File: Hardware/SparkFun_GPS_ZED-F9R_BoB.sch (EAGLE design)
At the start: 82 parts, among them J1 U.FL, J3 QWIIC_RIGHT_ANGLE, J4 QWIIC_RIGHT_ANGLE, U1 UBLOX_ZED_F9R, U2 3.3V, U4 HCPL-270L

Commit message: Renumbers parts, updates parts with PROD_IDs that didn't have them before
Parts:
- removed C12, C15: 1nF, SparkFun-Capacitors:1.0NF/1000PF-0402-25V-10%-X7R
- removed C16: 0.1uF, SparkFun-Capacitors:0.1UF-0402-6.3V-10%-X7R
- removed D10, D9: 0.5A/40V/420mV, classified:BZX84_DIODE
- removed R35, R37: 3.3k, SparkFun-Resistors:3.3KOHM-0603-1/10W-1%
- removed R36, R38: 470, SparkFun-Resistors:470OHM-0603-1/10W-1%
- removed R39, R40: 910, classified:910OHM-0603-1/10W-5%
- removed U$63: UHS_INVERTER_SCHMITT_TRIGGERSIP6, classified:UHS_INVERTER_SCHMITT_TRIGGERSIP6
- added C10, C9: 1.0uF, SparkFun-Capacitors:1.0UF-0603-16V-10%-X7R
- added C8: 47pF, SparkFun-Capacitors:47PF-0402-25V-5%-X7R
- added D7: BLUE, SparkFun-LED:LED-BLUE0603
- added D8: 0.5A/40V/420mV, SparkFun-DiscreteSemi:DIODE-SCHOTTKY-PMEG4005EJ
- added R29, R30: 1KOHM-0402-1/16W-1%, SparkFun-Resistors:1KOHM-0402-1/16W-1%
- added R31, R32: 27, SparkFun-Resistors:27OHM-0603-1/10W-1%
- added R33: 2.2K, SparkFun-Resistors:2.2KOHM-0402-1/16W-1%
- added R34: 3.3k, SparkFun-Resistors:3.3KOHM-0603-1/10W-1%
- added U5: 3.3V, SparkFun-IC-Power:V_REG_AP2112K-3.3V
- C1: value 1.0uF -> 0.1uF; device SparkFun-Capacitors:1.0UF-0603-16V-10%-X7R -> SparkFun-Capacitors:0.1UF-0402-6.3V-10%-X7R
- C2: value 47pF -> 1.0uF; device SparkFun-Capacitors:47PF-0402-25V-5%-X7R -> SparkFun-Capacitors:1.0UF-0603-16V-10%-X7R
- C3, C4: value 1.0uF -> 1nF; device SparkFun-Capacitors:1.0UF-0603-16V-10%-X7R -> SparkFun-Capacitors:1.0NF/1000PF-0402-25V-10%-X7R
- D1: value RED -> 0.5A/40V/420mV; device SparkFun-LED:LED-RED0603 -> classified:BZX84_DIODE
- D2: value BLUE -> 0.5A/40V/420mV; device SparkFun-LED:LED-BLUE0603 -> classified:BZX84_DIODE
- D3: value BLUE -> PRTR5V0U2F; device SparkFun-LED:LED-BLUE0603 -> SparkFun-IC-Power:PRTR5V0U2F
- D4: value BLUE -> RED; device SparkFun-LED:LED-BLUE0603 -> SparkFun-LED:LED-RED0603
- D5: value PRTR5V0U2F -> BLUE; device SparkFun-IC-Power:PRTR5V0U2F -> SparkFun-LED:LED-BLUE0603
- D6: value 0.5A/40V/420mV -> BLUE; device SparkFun-DiscreteSemi:DIODE-SCHOTTKY-PMEG4005EJ -> SparkFun-LED:LED-BLUE0603
- R1: value 100K -> 3.3k; device SparkFun-Resistors:100KOHM-0402-1/16W-1% -> SparkFun-Resistors:3.3KOHM-0603-1/10W-1%
- R17: device SparkFun-Resistors:33OHM-0603-1/10W-1% -> SparkFun-Resistors:33OHM-0402-1/10W-1%
- R18, R20: value 5.1k -> 33; device SparkFun-Resistors:5.1KOHM-0402-1/16W-1% -> SparkFun-Resistors:33OHM-0402-1/10W-1%
- R19: value 2.2K -> 33; device SparkFun-Resistors:2.2KOHM-0402-1/16W-1% -> SparkFun-Resistors:33OHM-0402-1/10W-1%
- R2: value 33 -> 3.3k; device SparkFun-Resistors:33OHM-0402-1/10W-1% -> SparkFun-Resistors:3.3KOHM-0603-1/10W-1%
- R21, R22: value 1KOHM-0402-1/16W-1% -> 33; device SparkFun-Resistors:1KOHM-0402-1/16W-1% -> SparkFun-Resistors:33OHM-0402-1/10W-1%
- R23: value 1KOHM-0402-1/16W-1% -> 33; device SparkFun-Resistors:1KOHM-0402-1/16W-1% -> SparkFun-Resistors:33OHM-0603-1/10W-1%
- R24: value 1KOHM-0402-1/16W-1% -> 5.1k; device SparkFun-Resistors:1KOHM-0402-1/16W-1% -> SparkFun-Resistors:5.1KOHM-0402-1/16W-1%
- R25: value 2.2K -> 5.1k; device SparkFun-Resistors:2.2KOHM-0402-1/16W-1% -> SparkFun-Resistors:5.1KOHM-0402-1/16W-1%
- R26: value 27 -> 2.2K; device SparkFun-Resistors:27OHM-0603-1/10W-1% -> SparkFun-Resistors:2.2KOHM-0402-1/16W-1%
- R27: value 27 -> 1KOHM-0402-1/16W-1%; device SparkFun-Resistors:27OHM-0603-1/10W-1% -> SparkFun-Resistors:1KOHM-0402-1/16W-1%
- R28: value 3.3k -> 1KOHM-0402-1/16W-1%; device SparkFun-Resistors:3.3KOHM-0603-1/10W-1% -> SparkFun-Resistors:1KOHM-0402-1/16W-1%
- R3: value 33 -> 100K; device SparkFun-Resistors:33OHM-0402-1/10W-1% -> SparkFun-Resistors:100KOHM-0402-1/16W-1%
- R4, R6: value 33 -> 910; device SparkFun-Resistors:33OHM-0402-1/10W-1% -> classified:910OHM-0603-1/10W-5%
- R5, R7: value 33 -> 470; device SparkFun-Resistors:33OHM-0402-1/10W-1% -> SparkFun-Resistors:470OHM-0603-1/10W-1%
- U1: value UBLOX_ZED_F9R -> HCPL-073L; device classified:UBLOX_ZED_F9R -> classified:HCPL-073L
- U2: value 3.3V -> UBLOX_ZED_F9R; device SparkFun-IC-Power:V_REG_AP2112K-3.3V -> classified:UBLOX_ZED_F9R
- U4: value HCPL-270L -> UHS_INVERTER_SCHMITT_TRIGGERSIP6; device classified:HCPL-270L -> classified:UHS_INVERTER_SCHMITT_TRIGGERSIP6
- renumbered $1_36_$_2020-02-13_17-32-45 to $1_25_$_2020-03-27_15-35-06, C17 to C6, C18 to C7, U$62 to U3
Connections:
- net !RESET: now also R10.2; no longer R4.2
- net !SAFEBOOT: now also R22.2; no longer R16.2
- net 3.3V: now also C10.1, C2.1, D4.A, D8.A, R3.2, R4.2, R6.2, U2.VCC, U2.V_USB, U5.OUT; no longer C16.1, C4.1, D1.A, D6.A, R1.2, R39.2, R40.2, U$63.VCC, U1.V_USB, U2.OUT
- net DIR+: now also R2.1; no longer R37.1
- net DIR_IN: now also R5.2, U1.ANODE2; no longer R38.2, U4.ANODE2
- net DIR_OUT: now also R9.1, U4.Y; no longer R3.1, U$63.Y
- net DIR_SCHMITT: now also R4.1, U1.VOUT2, U4.A; no longer R40.1, U$63.A, U4.VOUT2
- net DMINUS: now also R31.2, U2.USB_D-; no longer R26.2, U1.USB_D-
- net DPLUS: now also R32.2, U2.USB_D+; no longer R27.2, U1.USB_D+
- net D_SEL: now also U2.D_SEL; no longer U1.D_SEL
- net GEOF_STAT: now also D7.A, R19.2; no longer D4.A, R13.2
- net GND: now also C10.2, C8.2, C9.2, D1.A, D2.A, D3.2, R24.1, R25.1, R3.1, U1.CATHODE1, U1.CATHODE2, U5.GND; no longer C12.2, C15.2, C16.2, D10.A, D5.2, D9.A, R1.1, R18.1, R20.1, U$63.GND, U4.CATHODE1, U4.CATHODE2
- net INT: now also R11.2; no longer R5.2
- net N$1: now also R33.2; no longer R25.2
- net N$10: now also D3.4, R32.1; no longer D5.4, R27.1
- net N$11: now also R10.1, U2.!RESET!; no longer R4.1, U1.!RESET!
- net N$12: now also R11.1, U2.EXTINT; no longer R5.1, U1.EXTINT
- net N$14: now also R24.2; no longer R18.2
- net N$15: now also R25.2; no longer R20.2
- net N$16: now also R12.1, U2.SDA/!CS!; no longer R6.1, U1.SDA/!CS!
- net N$17: now also R13.1, U2.SCL/CLK; no longer R7.1, U1.SCL/CLK
- net N$18: now also R14.1, U2.TX_READY; no longer R8.1, U1.TX_READY
- net N$19: now also R15.1, U2.TX/MISO; no longer R9.1, U1.TX/MISO
- net N$2: now also D8.C, R34.2; no longer D6.C, R28.2
- net N$20: now also R16.1, U2.RX/MOSI; no longer R10.1, U1.RX/MOSI
- net N$21: now also R17.1, U2.TX2; no longer R11.1, U1.TX2
- net N$22: now also R29.1; no longer R23.1
- net N$23: now also R28.1; no longer R22.1
- net N$24: now also D5.C, R28.2; no longer D2.C, R22.2
- net N$25: now also D6.C, R29.2; no longer D3.C, R23.2
- net N$26: now also R18.1, U2.RX2; no longer R12.1, U1.RX2
- net N$27: now also R19.1, U2.GEO_FENCE_STAT; no longer R13.1, U1.GEO_FENCE_STAT
- net N$28: now also R20.1, U2.RTK_STAT; no longer R14.1, U1.RTK_STAT
- net N$29: now also R21.1, U2.TIMEPULSE; no longer R15.1, U1.TIMEPULSE
- net N$3: now also R26.2; no longer R19.2
- net N$30: now also R22.1, U2.!SAFEBOOT!; no longer R16.1, U1.!SAFEBOOT!
- net N$31: now also R8.2, U2.WHEEL_TKS; no longer R2.2, U1.WHEEL_TKS
- net N$32: now also R9.2, U2.DIR; no longer R3.2, U1.DIR
- net N$33: now also R30.1; no longer R24.1
- net N$34: now also D7.C, R30.2; no longer D4.C, R24.2
- net N$35: now also C4.1, D2.C, R1.2, R7.1; no longer C15.1, D9.C, R35.2, R36.1
- net N$37: now also C3.1, D1.C, R2.2, R5.1; no longer C12.1, D10.C, R37.2, R38.1
- net N$4: now also D4.C, R27.2; no longer D1.C, R21.2
- net N$5: now also C8.1, R23.1; no longer C2.1, R17.1
- net N$6: now also D3.3; no longer D5.3
- net N$7: now also D3.1; no longer D5.1
- net N$8: now also R27.1; no longer R21.1
- net N$9: now also D3.6, R31.1; no longer D5.6, R26.1
- net PPS: now also D5.A, R21.2; no longer D2.A, R15.2
- net RF_IN: now also U2.RF_IN; no longer U1.RF_IN
- net RTK_STAT: now also D6.A, R20.2; no longer D3.A, R14.2
- net RXI/MOSI: now also R16.2; no longer R10.2
- net RXI2: now also R18.2; no longer R12.2
- net SCL/CLK: now also R13.2, R26.1; no longer R19.1, R7.2
- net SDA/!CS: now also R12.2, R33.1; no longer R25.1, R6.2
- net TXO/MISO: now also R15.2; no longer R9.2
- net TXO2: now also R17.2; no longer R11.2
- net TX_READY: now also R14.2; no longer R8.2
- net VIN: now also C9.1, D3.5, U5.EN, U5.IN; no longer C3.1, D5.5, U2.EN, U2.IN
- net V_BATT: now also R34.1, U2.V_BKCP; no longer R28.1, U1.V_BKCP
- net V_RF: now also R23.2, U2.V_RF; no longer R17.2, U1.V_RF
- net WT+: now also R1.1; no longer R35.1
- net WT_IN: now also R7.2, U1.ANODE1; no longer R36.2, U4.ANODE1
- net WT_OUT: now also R8.1; no longer R2.1
- net WT_SCHMITT: now also R6.1, U1.VOUT1; no longer R39.1, U4.VOUT1
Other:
- moved on the sheet: C1, C2, C3, C4, D4, R1, R10, R11, R12, R13, R14, R15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

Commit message: Updates silk, fixes RF trace, moves some traces for better clearance
* Fixes various small design issues
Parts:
- renumbered JP1 to PWR, JP2 to PPS, JP3 to RTK, JP4 to GEOF
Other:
- note added: "Wheel Tick/Direction Input: 3-24V"

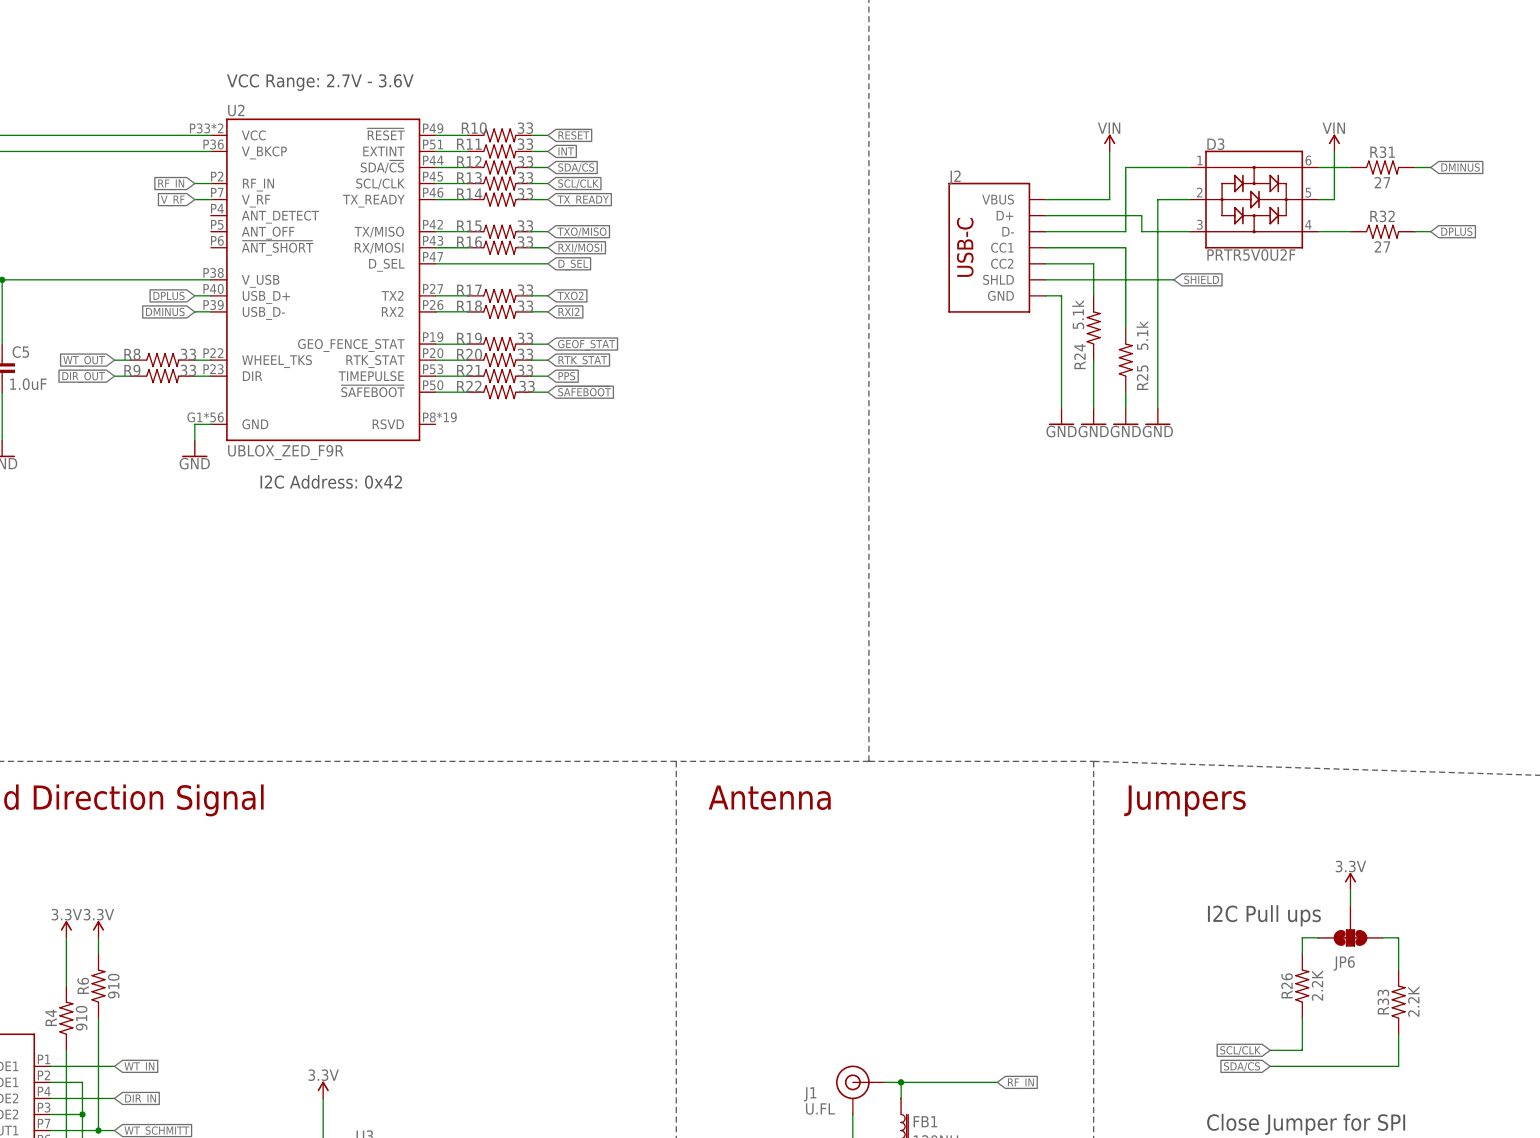
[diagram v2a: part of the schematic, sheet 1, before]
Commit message: Removes 0402 33 Ohm resistors in place of 33Ohm resistor bank
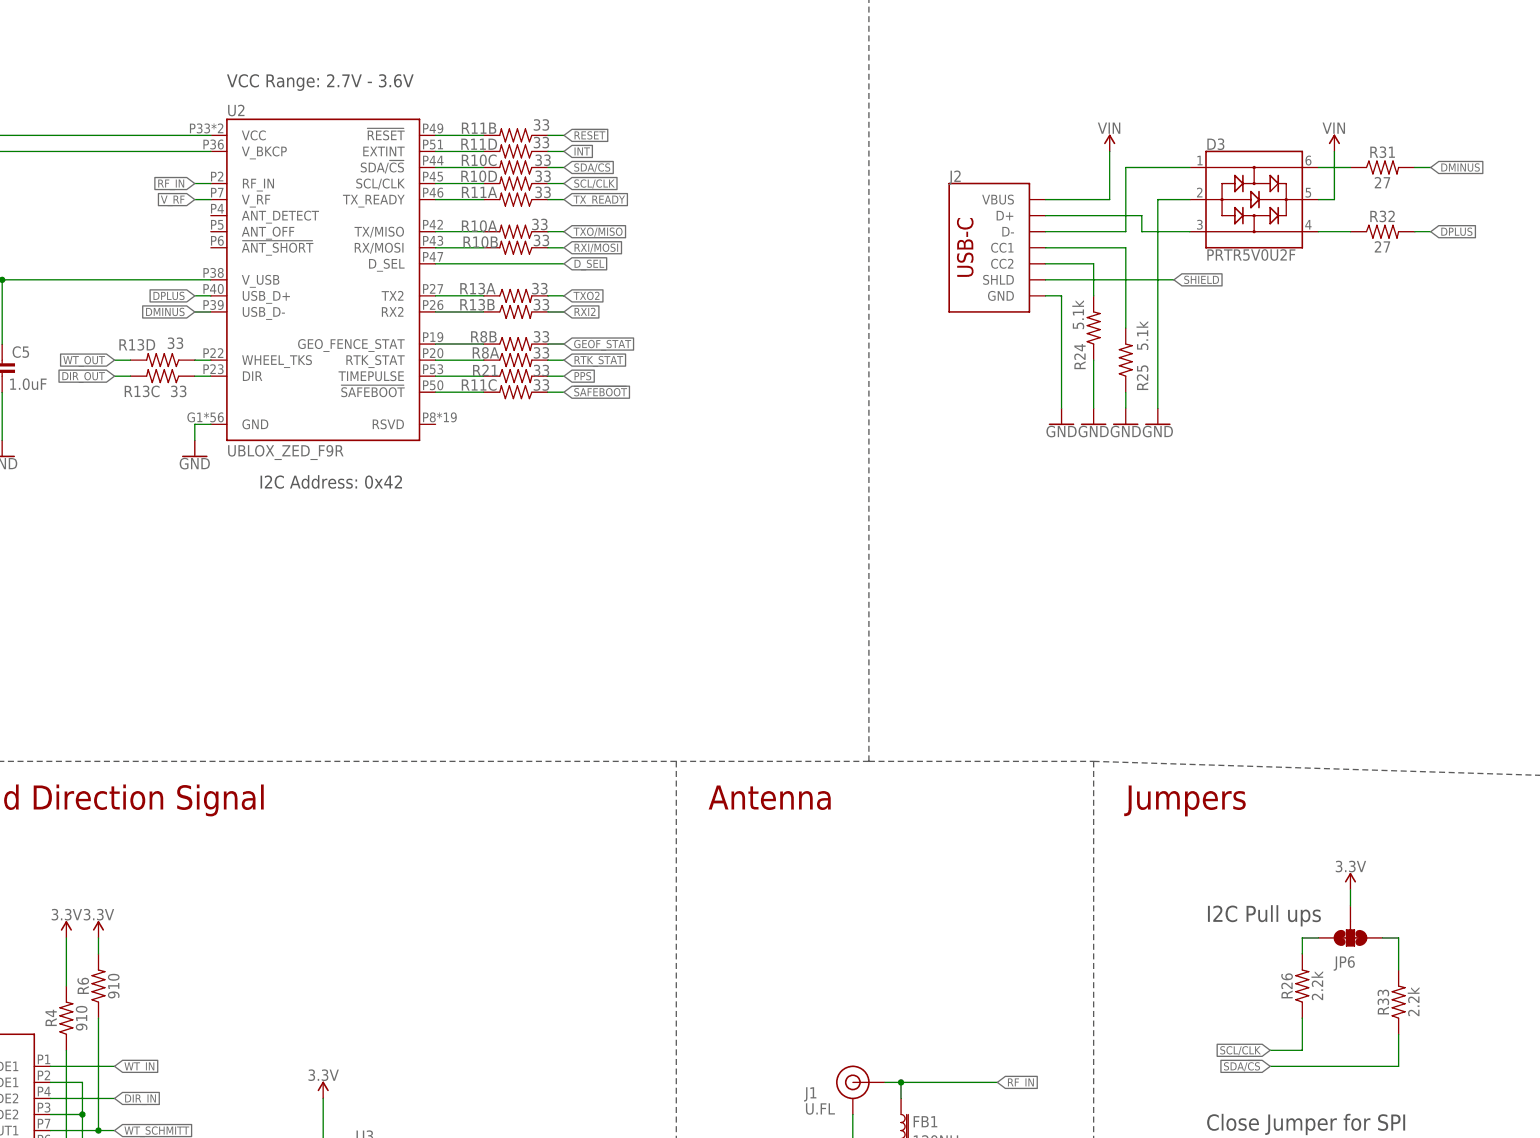
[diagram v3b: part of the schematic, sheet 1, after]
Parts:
- removed R12, R14, R15, R16, R17, R18, R19, R20, R22, R9: 33, SparkFun-Resistors:33OHM-0402-1/10W-1%
- R10, R11, R13, R8: device SparkFun-Resistors:33OHM-0402-1/10W-1% -> SparkFun-Resistors:33OHM_RESISTOR_ARRAY
- R21: device SparkFun-Resistors:33OHM-0402-1/10W-1% -> SparkFun-Resistors:33OHM-0603-1/10W-1%
- R26, R33: value 2.2K -> 2.2k; device SparkFun-Resistors:2.2KOHM-0402-1/16W-1% -> SparkFun-Resistors:2.2KOHM-0603-1/10W-1%
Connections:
- net !RESET: now also R11B.1; no longer R10.2
- net !SAFEBOOT: now also R11C.1; no longer R22.2
- net DIR_OUT: now also R13C.2; no longer R9.1
- net GEOF_STAT: now also R8B.2; no longer R19.2
- net INT: now also R11D.1; no longer R11.2
- net N$11: now also R11B.2; no longer R10.1
- net N$12: now also R11D.2; no longer R11.1
- net N$16: now also R10C.2; no longer R12.1
- net N$17: now also R10D.2; no longer R13.1
- net N$18: now also R11A.2; no longer R14.1
- net N$19: now also R10A.2; no longer R15.1
- net N$20: now also R10B.2; no longer R16.1
- net N$21: now also R13A.1; no longer R17.1
- net N$26: now also R13B.1; no longer R18.1
- net N$27: now also R8B.1; no longer R19.1
- net N$28: now also R8A.1; no longer R20.1
- net N$30: now also R11C.2; no longer R22.1
- net N$31: now also R13D.1; no longer R8.2
- net N$32: now also R13C.1; no longer R9.2
- net RTK_STAT: now also R8A.2; no longer R20.2
- net RXI/MOSI: now also R10B.1; no longer R16.2
- net RXI2: now also R13B.2; no longer R18.2
- net SCL/CLK: now also R10D.1; no longer R13.2
- net SDA/!CS: now also R10C.1; no longer R12.2
- net TXO/MISO: now also R10A.1; no longer R15.2
- net TXO2: now also R13A.2; no longer R17.2
- net TX_READY: now also R11A.1; no longer R14.2
- net WT_OUT: now also R13D.2; no longer R8.1
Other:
- moved on the sheet: R21

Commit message: Fixes packages with over sized tnames and tvalues
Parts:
- removed R31: 27, SparkFun-Resistors:27OHM-0603-1/10W-1%
- removed R33: 2.2k, SparkFun-Resistors:2.2KOHM-0603-1/10W-1%
- removed R34: 3.3k, SparkFun-Resistors:3.3KOHM-0603-1/10W-1%
- added R12: 33, SparkFun-Resistors:33OHM-0603-1/10W-1%
- added R14: 5.1k, SparkFun-Resistors:5.1KOHM-0402-1/16W-1%
- added R9: 33, SparkFun-Resistors:33OHM_RESISTOR_ARRAY
- R13: device SparkFun-Resistors:33OHM_RESISTOR_ARRAY -> SparkFun-Resistors:33OHM-0603-1/10W-1%
- R21: value 33 -> 27; device SparkFun-Resistors:33OHM-0603-1/10W-1% -> SparkFun-Resistors:27OHM-0603-1/10W-1%
- R23: value 33 -> 2.2k; device SparkFun-Resistors:33OHM-0603-1/10W-1% -> SparkFun-Resistors:2.2KOHM-0603-1/10W-1%
- R24: value 5.1k -> 3.3k; device SparkFun-Resistors:5.1KOHM-0402-1/16W-1% -> SparkFun-Resistors:3.3KOHM-0603-1/10W-1%
- R6: value 910 -> 470; device classified:910OHM-0603-1/10W-5% -> SparkFun-Resistors:470OHM-0603-1/10W-1%
- R7: value 470 -> 910; device SparkFun-Resistors:470OHM-0603-1/10W-1% -> classified:910OHM-0603-1/10W-5%
- renumbered $1_25_$_2020-03-27_15-35-06 to $1_25_$_2020-03-30_22-47-33, GEOF to JP4, PPS to JP2, PWR to JP1, R25 to R15, R26 to R16, R27 to R17, R28 to R18, R29 to R19, R30 to R20, R32 to R22, RTK to JP3
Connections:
- net !RESET: now also R8B.1; no longer R11B.1
- net !SAFEBOOT: now also R8C.1; no longer R11C.1
- net 3.3V: now also R7.2; no longer R6.2
- net DIR+: now also R1.1; no longer R2.1
- net DIR_OUT: now also R10C.2; no longer R13C.2
- net DMINUS: now also R21.2; no longer R31.2
- net GEOF_STAT: now also R11B.2; no longer R8B.2
- net GND: now also R14.1; no longer R24.1
- net INT: now also R8D.1; no longer R11D.1
- net N$1: now also R23.2; no longer R33.2
- net N$11: now also R8B.2; no longer R11B.2
- net N$12: now also R8D.2; no longer R11D.2
- net N$14: now also R14.2; no longer R24.2
- net N$16: now also R9C.2; no longer R10C.2
- net N$17: now also R9D.2; no longer R10D.2
- net N$18: now also R8A.2; no longer R11A.2
- net N$19: now also R9A.2; no longer R10A.2
- net N$2: now also R24.2; no longer R34.2
- net N$20: now also R9B.2; no longer R10B.2
- net N$21: now also R10A.1; no longer R13A.1
- net N$26: now also R10B.1; no longer R13B.1
- net N$27: now also R11B.1; no longer R8B.1
- net N$28: now also R11A.1; no longer R8A.1
- net N$29: now also R12.1; no longer R21.1
- net N$30: now also R8C.2; no longer R11C.2
- net N$31: now also R10D.1; no longer R13D.1
- net N$32: now also R10C.1; no longer R13C.1
- net N$35: now also R2.2, R6.1; no longer R1.2, R7.1
- net N$37: now also R1.2; no longer R2.2
- net N$5: now also R13.1; no longer R23.1
- net N$9: now also R21.1; no longer R31.1
- net PPS: now also R12.2; no longer R21.2
- net RTK_STAT: now also R11A.2; no longer R8A.2
- net RXI/MOSI: now also R9B.1; no longer R10B.1
- net RXI2: now also R10B.2; no longer R13B.2
- net SCL/CLK: now also R9D.1; no longer R10D.1
- net SDA/!CS: now also R23.1, R9C.1; no longer R10C.1, R33.1
- net TXO/MISO: now also R9A.1; no longer R10A.1
- net TXO2: now also R10A.2; no longer R13A.2
- net TX_READY: now also R8A.1; no longer R11A.1
- net V_BATT: now also R24.1; no longer R34.1
- net V_RF: now also R13.2; no longer R23.2
- net WT+: now also R2.1; no longer R1.1
- net WT_IN: now also R6.2; no longer R7.2
- net WT_OUT: now also R10D.2; no longer R13D.2
- net WT_SCHMITT: now also R7.1; no longer R6.1
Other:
- moved on the sheet: R1, R10A, R10B, R10C, R10D, R11A, R11B, R2, R21, R23, R6, R7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

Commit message: Fixes more tvalues and tnames
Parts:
- renumbered $1_25_$_2020-03-30_22-47-33 to $1_25_$_2020-03-30_22-52-05
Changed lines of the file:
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@@
 <part name="FD4" library="SparkFun-Aesthetics" deviceset="FIDUCIAL" device="UFIDUCIAL" value="FIDUCIALUFIDUCIAL"/>
 <part name="FD1" library="SparkFun-Aesthetics" deviceset="FIDUCIAL" device="UFIDUCIAL" value="FIDUCIALUFIDUCIAL"/>
-<part name="$1_25_$_2020-03-30_22-47-33" library="SparkFun-Hardware" deviceset="STAND-OFF" device="TIGHT"/>
+<part name="$1_25_$_2020-03-30_22-52-05" library="SparkFun-Hardware" deviceset="STAND-OFF" device="TIGHT"/>
 <part name="H2" library="SparkFun-Hardware" deviceset="STAND-OFF" device="TIGHT"/>
 <part name="JP5" library="SparkFun-Jumpers" deviceset="JUMPER-SMT_2_NO" device="_SILK" package3d_urn="urn:adsk.eagle:package:39279/1"/>
@@
 <instance part="FD4" gate="G$1" x="426.72" y="30.48" smashed="yes"/>
 <instance part="FD1" gate="G$1" x="424.18" y="33.02" smashed="yes"/>
-<instance part="$1_25_$_2020-03-30_22-47-33" gate="G$1" x="411.48" y="33.02" smashed="yes"/>
+<instance part="$1_25_$_2020-03-30_22-52-05" gate="G$1" x="411.48" y="33.02" smashed="yes"/>
 <instance part="H2" gate="G$1" x="411.48" y="30.48" smashed="yes"/>
 <instance part="JP5" gate="G$1" x="248.92" y="68.58" smashed="yes">
